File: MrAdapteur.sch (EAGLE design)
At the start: 12 parts, among them J1 PIN2F061.080, J2 PIN2F061.080, X1 1751248

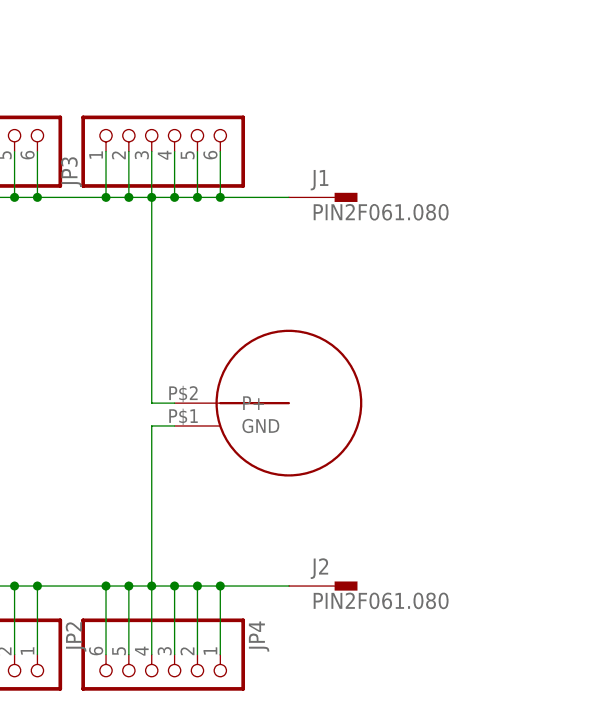
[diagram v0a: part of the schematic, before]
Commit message: Added standard DC jack, 4.75mm flat connector and wire loop for attaching alligator clips or scope probes
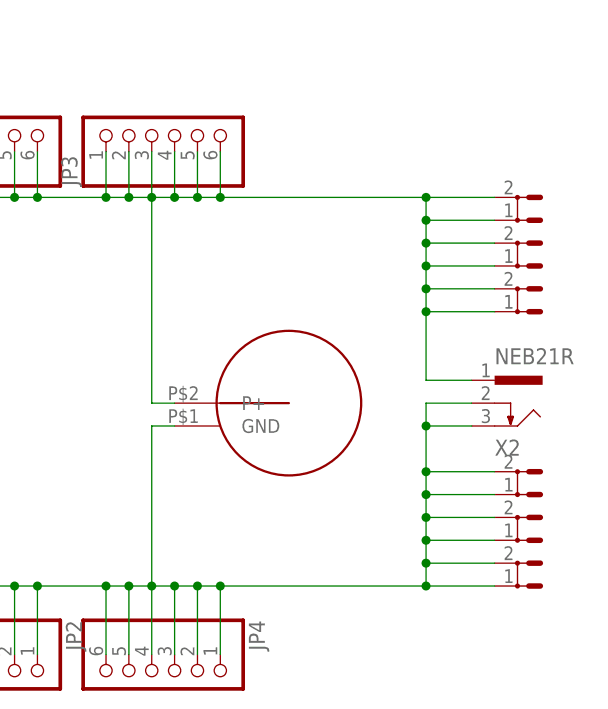
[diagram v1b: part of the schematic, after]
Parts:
- removed J1, J2: PIN2F061.080, con-faston:PIN2F061.080
- added X2: NEB21R, con-lumberg:NEB21R
- added X3, X4, X5, X6, X7, X8: (no value), con-rib:ST4,8
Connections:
- net N$1: now also X2.1, X3.1, X3.2, X5.1, X5.2, X7.1, X7.2; no longer J1.1
- net N$3: now also X2.2, X2.3, X4.1, X4.2, X6.1, X6.2, X8.1, X8.2; no longer J2.1
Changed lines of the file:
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@@
 <attribute name="OC_TME" value="ZL262-6SG"/>
 </part>
-<part name="J1" library="con-faston" deviceset="PIN2" device="F061.080">
-<attribute name="OC_TME" value="FS1536"/>
-</part>
-<part name="J2" library="con-faston" deviceset="PIN2" device="F061.080">
-<attribute name="OC_TME" value="FS1536"/>
-</part>
 <part name="X1" library="con-phoenix-350" deviceset="1751248" device=""/>
+<part name="X2" library="con-lumberg" deviceset="NEB21R" device=""/>
+<part name="X3" library="con-rib" deviceset="ST4,8" device=""/>
+<part name="X4" library="con-rib" deviceset="ST4,8" device=""/>
+<part name="X5" library="con-rib" deviceset="ST4,8" device=""/>
+<part name="X6" library="con-rib" deviceset="ST4,8" device=""/>
+<part name="X7" library="con-rib" deviceset="ST4,8" device=""/>
+<part name="X8" library="con-rib" deviceset="ST4,8" device=""/>
 </parts>
 <sheets>
@@
 <attribute name="OC_TME" x="116.84" y="30.48" size="1.778" layer="96" rot="R270" display="off"/>
 </instance>
-<instance part="J1" gate="-1" x="137.16" y="83.82">
-<attribute name="OC_TME" x="137.16" y="83.82" size="1.778" layer="96" display="off"/>
-</instance>
-<instance part="J2" gate="-1" x="137.16" y="40.64">
-<attribute name="OC_TME" x="137.16" y="40.64" size="1.778" layer="96" display="off"/>
-</instance>
 <instance part="X1" gate="-1" x="40.64" y="83.82" rot="R180"/>
 <instance part="X1" gate="-2" x="40.64" y="40.64" rot="R180"/>
+<instance part="X2" gate="G$1" x="157.48" y="60.96" rot="MR180"/>
+<instance part="X3" gate="-1" x="160.02" y="78.74" smashed="yes" rot="R180">
+<attribute name="VALUE" x="160.02" y="81.153" size="1.778" layer="96" rot="R180"/>
+</instance>
+<instance part="X4" gate="-1" x="160.02" y="48.26" smashed="yes" rot="R180">
+<attribute name="VALUE" x="160.02" y="50.673" size="1.778" layer="96" rot="R180"/>
+</instance>
+<instance part="X5" gate="-1" x="160.02" y="73.66" smashed="yes" rot="R180">
+<attribute name="VALUE" x="160.02" y="76.073" size="1.778" layer="96" rot="R180"/>
+</instance>
+<instance part="X6" gate="-1" x="160.02" y="53.34" smashed="yes" rot="R180">
+<attribute name="VALUE" x="160.02" y="55.753" size="1.778" layer="96" rot="R180"/>
+</instance>
+<instance part="X7" gate="-1" x="160.02" y="83.82" smashed="yes" rot="R180">
+<attribute name="VALUE" x="160.02" y="86.233" size="1.778" layer="96" rot="R180"/>
+</instance>
+<instance part="X8" gate="-1" x="160.02" y="43.18" smashed="yes" rot="R180">
+<attribute name="VALUE" x="160.02" y="45.593" size="1.778" layer="96" rot="R180"/>
+</instance>
 </instances>
 <busses>
@@
 <wire x1="114.3" y1="88.9" x2="114.3" y2="83.82" width="0.1524" layer="91"/>
 <junction x="114.3" y="83.82"/>
-<pinref part="J1" gate="-1" pin="1"/>
-<wire x1="124.46" y1="83.82" x2="132.08" y2="83.82" width="0.1524" layer="91"/>
+<wire x1="124.46" y1="83.82" x2="147.32" y2="83.82" width="0.1524" layer="91"/>
 <junction x="124.46" y="83.82"/>
 <pinref part="X1" gate="-1" pin="K"/>
 <junction x="43.18" y="83.82"/>
+<pinref part="X2" gate="G$1" pin="1"/>
+<wire x1="147.32" y1="83.82" x2="154.94" y2="83.82" width="0.1524" layer="91"/>
+<wire x1="152.4" y1="63.5" x2="147.32" y2="63.5" width="0.1524" layer="91"/>
+<wire x1="147.32" y1="63.5" x2="147.32" y2="71.12" width="0.1524" layer="91"/>
+<junction x="147.32" y="83.82"/>
+<pinref part="X3" gate="-1" pin="2"/>
+<wire x1="147.32" y1="71.12" x2="147.32" y2="73.66" width="0.1524" layer="91"/>
+<wire x1="147.32" y1="73.66" x2="147.32" y2="76.2" width="0.1524" layer="91"/>
+<wire x1="147.32" y1="76.2" x2="147.32" y2="78.74" width="0.1524" layer="91"/>
+<wire x1="147.32" y1="78.74" x2="147.32" y2="81.28" width="0.1524" layer="91"/>
+<wire x1="147.32" y1="81.28" x2="147.32" y2="83.82" width="0.1524" layer="91"/>
+<wire x1="154.94" y1="78.74" x2="147.32" y2="78.74" width="0.1524" layer="91"/>
+<junction x="147.32" y="78.74"/>
+<pinref part="X3" gate="-1" pin="1"/>
+<wire x1="154.94" y1="76.2" x2="147.32" y2="76.2" width="0.1524" layer="91"/>
+<junction x="147.32" y="76.2"/>
+<pinref part="X5" gate="-1" pin="2"/>
+<wire x1="154.94" y1="73.66" x2="147.32" y2="73.66" width="0.1524" layer="91"/>
+<junction x="147.32" y="73.66"/>
+<pinref part="X5" gate="-1" pin="1"/>
+<wire x1="154.94" y1="71.12" x2="147.32" y2="71.12" width="0.1524" layer="91"/>
+<junction x="147.32" y="71.12"/>
+<pinref part="X7" gate="-1" pin="2"/>
+<pinref part="X7" gate="-1" pin="1"/>
+<wire x1="154.94" y1="81.28" x2="147.32" y2="81.28" width="0.1524" layer="91"/>
+<junction x="147.32" y="81.28"/>
 </segment>
 </net>
@@
 <pinref part="JP4" gate="A" pin="1"/>
 <wire x1="124.46" y1="33.02" x2="124.46" y2="40.64" width="0.1524" layer="91"/>
-<pinref part="J2" gate="-1" pin="1"/>
-<wire x1="124.46" y1="40.64" x2="132.08" y2="40.64" width="0.1524" layer="91"/>
+<wire x1="124.46" y1="40.64" x2="147.32" y2="40.64" width="0.1524" layer="91"/>
 <junction x="124.46" y="40.64"/>
 <pinref part="X1" gate="-2" pin="K"/>
 <junction x="43.18" y="40.64"/>
+<pinref part="X2" gate="G$1" pin="2"/>
+<wire x1="147.32" y1="40.64" x2="154.94" y2="40.64" width="0.1524" layer="91"/>
+<wire x1="152.4" y1="60.96" x2="147.32" y2="60.96" width="0.1524" layer="91"/>
+<wire x1="147.32" y1="60.96" x2="147.32" y2="58.42" width="0.1524" layer="91"/>
+<junction x="147.32" y="40.64"/>
+<pinref part="X2" gate="G$1" pin="3"/>
+<wire x1="147.32" y1="58.42" x2="147.32" y2="53.34" width="0.1524" layer="91"/>
+<wire x1="147.32" y1="53.34" x2="147.32" y2="50.8" width="0.1524" layer="91"/>
+<wire x1="147.32" y1="50.8" x2="147.32" y2="48.26" width="0.1524" layer="91"/>
+<wire x1="147.32" y1="48.26" x2="147.32" y2="45.72" width="0.1524" layer="91"/>
+<wire x1="147.32" y1="45.72" x2="147.32" y2="43.18" width="0.1524" layer="91"/>
+<wire x1="147.32" y1="43.18" x2="147.32" y2="40.64" width="0.1524" layer="91"/>
+<wire x1="152.4" y1="58.42" x2="147.32" y2="58.42" width="0.1524" layer="91"/>
+<junction x="147.32" y="58.42"/>
+<pinref part="X4" gate="-1" pin="2"/>
+<wire x1="154.94" y1="48.26" x2="147.32" y2="48.26" width="0.1524" layer="91"/>
+<junction x="147.32" y="48.26"/>
+<pinref part="X4" gate="-1" pin="1"/>
+<wire x1="154.94" y1="45.72" x2="147.32" y2="45.72" width="0.1524" layer="91"/>
+<junction x="147.32" y="45.72"/>
+<pinref part="X6" gate="-1" pin="2"/>
+<wire x1="154.94" y1="53.34" x2="147.32" y2="53.34" width="0.1524" layer="91"/>
+<junction x="147.32" y="53.34"/>
+<pinref part="X6" gate="-1" pin="1"/>
+<wire x1="154.94" y1="50.8" x2="147.32" y2="50.8" width="0.1524" layer="91"/>
+<junction x="147.32" y="50.8"/>
+<pinref part="X8" gate="-1" pin="2"/>
+<wire x1="154.94" y1="43.18" x2="147.32" y2="43.18" width="0.1524" layer="91"/>
+<junction x="147.32" y="43.18"/>
+<pinref part="X8" gate="-1" pin="1"/>
 </segment>
 </net>

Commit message: Replaced DC connector with the adafruit one for bigger holes
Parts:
- removed X2: NEB21R, con-lumberg:NEB21R
- added U$6: 2.1MMJACKTHM, adafruit:2.1MMJACKTHM
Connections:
- net N$1: now also U$6.TIP; no longer X2.1
- net N$3: now also U$6.RING, U$6.RING_SW; no longer X2.2, X2.3
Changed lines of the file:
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@@
 <layer number="48" name="Document" color="7" fill="1" visible="no" active="no"/>
 <layer number="49" name="Reference" color="7" fill="1" visible="no" active="no"/>
+<layer number="50" name="dxf" color="7" fill="1" visible="no" active="no"/>
 <layer number="51" name="tDocu" color="7" fill="1" visible="no" active="no"/>
 <layer number="52" name="bDocu" color="7" fill="1" visible="no" active="no"/>
+<layer number="53" name="tGND_GNDA" color="7" fill="9" visible="no" active="no"/>
+<layer number="54" name="bGND_GNDA" color="1" fill="9" visible="no" active="no"/>
+<layer number="56" name="wert" color="7" fill="1" visible="no" active="no"/>
+<layer number="57" name="tCAD" color="7" fill="1" visible="no" active="no"/>
 <layer number="91" name="Nets" color="2" fill="1" visible="yes" active="yes"/>
 <layer number="92" name="Busses" color="1" fill="1" visible="yes" active="yes"/>
@@
 <layer number="97" name="Info" color="7" fill="1" visible="yes" active="yes"/>
 <layer number="98" name="Guide" color="6" fill="1" visible="yes" active="yes"/>
+<layer number="100" name="Muster" color="7" fill="1" visible="no" active="no"/>
+<layer number="101" name="Patch_Top" color="12" fill="4" visible="yes" active="yes"/>
+<layer number="102" name="Vscore" color="7" fill="1" visible="yes" active="yes"/>
+<layer number="103" name="fp3" color="7" fill="1" visible="no" active="yes"/>
+<layer number="104" name="Name" color="7" fill="1" visible="yes" active="yes"/>
+<layer number="105" name="Beschreib" color="9" fill="1" visible="yes" active="yes"/>
+<layer number="106" name="BGA-Top" color="4" fill="1" visible="yes" active="yes"/>
+<layer number="107" name="BD-Top" color="5" fill="1" visible="yes" active="yes"/>
+<layer number="108" name="fp8" color="7" fill="1" visible="no" active="yes"/>
+<layer number="109" name="fp9" color="7" fill="1" visible="no" active="yes"/>
+<layer number="110" name="fp0" color="7" fill="1" visible="no" active="yes"/>
+<layer number="111" name="LPC17xx" color="7" fill="1" visible="yes" active="yes"/>
+<layer number="112" name="tSilk" color="7" fill="1" visible="yes" active="yes"/>
+<layer number="116" name="Patch_BOT" color="9" fill="4" visible="yes" active="yes"/>
+<layer number="121" name="_tsilk" color="7" fill="1" visible="yes" active="yes"/>
+<layer number="122" name="_bsilk" color="7" fill="1" visible="yes" active="yes"/>
+<layer number="123" name="tTestmark" color="7" fill="1" visible="no" active="yes"/>
+<layer number="124" name="bTestmark" color="7" fill="1" visible="no" active="yes"/>
+<layer number="125" name="_tNames" color="7" fill="1" visible="yes" active="yes"/>
+<layer number="126" name="_bNames" color="7" fill="1" visible="yes" active="yes"/>
+<layer number="127" name="_tValues" color="7" fill="1" visible="yes" active="yes"/>
+<layer number="128" name="_bValues" color="7" fill="1" visible="yes" active="yes"/>
+<layer number="131" name="tAdjust" color="7" fill="1" visible="no" active="yes"/>
+<layer number="132" name="bAdjust" color="7" fill="1" visible="no" active="yes"/>
+<layer number="144" name="Drill_legend" color="7" fill="1" visible="yes" active="yes"/>
+<layer number="150" name="Notes" color="7" fill="1" visible="no" active="yes"/>
+<layer number="151" name="HeatSink" color="7" fill="1" visible="yes" active="yes"/>
+<layer number="152" name="_bDocu" color="7" fill="1" visible="yes" active="yes"/>
+<layer number="153" name="FabDoc1" color="6" fill="1" visible="no" active="no"/>
+<layer number="154" name="FabDoc2" color="2" fill="1" visible="no" active="no"/>
+<layer number="155" name="FabDoc3" color="7" fill="15" visible="no" active="no"/>
+<layer number="199" name="Contour" color="7" fill="1" visible="yes" active="yes"/>
+<layer number="200" name="200bmp" color="1" fill="10" visible="yes" active="yes"/>
+<layer number="201" name="201bmp" color="2" fill="1" visible="no" active="no"/>
+<layer number="202" name="202bmp" color="3" fill="1" visible="no" active="no"/>
+<layer number="203" name="203bmp" color="4" fill="10" visible="yes" active="yes"/>
+<layer number="204" name="204bmp" color="5" fill="10" visible="yes" active="yes"/>
+<layer number="205" name="205bmp" color="6" fill="10" visible="yes" active="yes"/>
+<layer number="206" name="206bmp" color="7" fill="10" visible="yes" active="yes"/>
+<layer number="207" name="207bmp" color="8" fill="10" visible="yes" active="yes"/>
+<layer number="208" name="208bmp" color="9" fill="10" visible="yes" active="yes"/>
+<layer number="209" name="209bmp" color="7" fill="1" visible="no" active="yes"/>
+<layer number="210" name="210bmp" color="7" fill="1" visible="no" active="yes"/>
+<layer number="211" name="211bmp" color="7" fill="1" visible="yes" active="yes"/>
+<layer number="212" name="212bmp" color="7" fill="1" visible="yes" active="yes"/>
+<layer number="213" name="213bmp" color="7" fill="1" visible="yes" active="yes"/>
+<layer number="214" name="214bmp" color="7" fill="1" visible="yes" active="yes"/>
+<layer number="215" name="215bmp" color="7" fill="1" visible="yes" active="yes"/>
+<layer number="216" name="216bmp" color="7" fill="1" visible="yes" active="yes"/>
+<layer number="217" name="217bmp" color="18" fill="1" visible="no" active="no"/>
+<layer number="218" name="218bmp" color="19" fill="1" visible="no" active="no"/>
+<layer number="219" name="219bmp" color="20" fill="1" visible="no" active="no"/>
+<layer number="220" name="220bmp" color="21" fill="1" visible="no" active="no"/>
+<layer number="221" name="221bmp" color="22" fill="1" visible="no" active="no"/>
+<layer number="222" name="222bmp" color="23" fill="1" visible="no" active="no"/>
+<layer number="223" name="223bmp" color="24" fill="1" visible="no" active="no"/>
+<layer number="224" name="224bmp" color="25" fill="1" visible="no" active="no"/>
+<layer number="248" name="Housing" color="7" fill="1" visible="yes" active="yes"/>
+<layer number="249" name="Edge" color="7" fill="1" visible="yes" active="yes"/>
+<layer number="250" name="Descript" color="7" fill="1" visible="no" active="no"/>
+<layer number="251" name="SMDround" color="7" fill="1" visible="no" active="no"/>
+<layer number="254" name="cooling" color="7" fill="1" visible="yes" active="yes"/>
 </layers>
 <schematic xreflabel="%F%N/%S.%C%R" xrefpart="/%S.%C%R">
@@
 </part>
 <part name="X1" library="con-phoenix-350" deviceset="1751248" device=""/>
-<part name="X2" library="con-lumberg" deviceset="NEB21R" device=""/>
 <part name="X3" library="con-rib" deviceset="ST4,8" device=""/>
 <part name="X4" library="con-rib" deviceset="ST4,8" device=""/>
@@
 <part name="X7" library="con-rib" deviceset="ST4,8" device=""/>
 <part name="X8" library="con-rib" deviceset="ST4,8" device=""/>
+<part name="U$6" library="adafruit" deviceset="2.1MMJACK" device="THM"/>
 </parts>
 <sheets>
@@
 <instance part="X1" gate="-1" x="40.64" y="83.82" rot="R180"/>
 <instance part="X1" gate="-2" x="40.64" y="40.64" rot="R180"/>
-<instance part="X2" gate="G$1" x="157.48" y="60.96" rot="MR180"/>
 <instance part="X3" gate="-1" x="160.02" y="78.74" smashed="yes" rot="R180">
 <attribute name="VALUE" x="160.02" y="81.153" size="1.778" layer="96" rot="R180"/>
@@
 <attribute name="VALUE" x="160.02" y="45.593" size="1.778" layer="96" rot="R180"/>
 </instance>
+<instance part="U$6" gate="G$1" x="157.48" y="60.96" rot="MR0"/>
 </instances>
 <busses>
@@
 <pinref part="X1" gate="-1" pin="K"/>
 <junction x="43.18" y="83.82"/>
-<pinref part="X2" gate="G$1" pin="1"/>
 <wire x1="147.32" y1="83.82" x2="154.94" y2="83.82" width="0.1524" layer="91"/>
 <wire x1="152.4" y1="63.5" x2="147.32" y2="63.5" width="0.1524" layer="91"/>
@@
 <wire x1="154.94" y1="81.28" x2="147.32" y2="81.28" width="0.1524" layer="91"/>
 <junction x="147.32" y="81.28"/>
+<pinref part="U$6" gate="G$1" pin="TIP"/>
 </segment>
 </net>
@@
 <pinref part="X1" gate="-2" pin="K"/>
 <junction x="43.18" y="40.64"/>
-<pinref part="X2" gate="G$1" pin="2"/>
 <wire x1="147.32" y1="40.64" x2="154.94" y2="40.64" width="0.1524" layer="91"/>
 <wire x1="152.4" y1="60.96" x2="147.32" y2="60.96" width="0.1524" layer="91"/>
 <wire x1="147.32" y1="60.96" x2="147.32" y2="58.42" width="0.1524" layer="91"/>
 <junction x="147.32" y="40.64"/>
-<pinref part="X2" gate="G$1" pin="3"/>
 <wire x1="147.32" y1="58.42" x2="147.32" y2="53.34" width="0.1524" layer="91"/>
 <wire x1="147.32" y1="53.34" x2="147.32" y2="50.8" width="0.1524" layer="91"/>
@@
 <junction x="147.32" y="43.18"/>
 <pinref part="X8" gate="-1" pin="1"/>
+<pinref part="U$6" gate="G$1" pin="RING"/>
+<pinref part="U$6" gate="G$1" pin="RING_SW"/>
 </segment>
 </net>

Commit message: Several minor fixes (sorry, can't remember them) ;)
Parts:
- removed X7, X8: (no value), con-rib:ST4,8
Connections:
- net N$1: no longer X7.1, X7.2
- net N$3: no longer X8.1, X8.2
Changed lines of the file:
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@@
 <part name="X5" library="con-rib" deviceset="ST4,8" device=""/>
 <part name="X6" library="con-rib" deviceset="ST4,8" device=""/>
-<part name="X7" library="con-rib" deviceset="ST4,8" device=""/>
-<part name="X8" library="con-rib" deviceset="ST4,8" device=""/>
 <part name="U$6" library="adafruit" deviceset="2.1MMJACK" device="THM"/>
 </parts>
@@
 <instance part="X6" gate="-1" x="160.02" y="53.34" smashed="yes" rot="R180">
 <attribute name="VALUE" x="160.02" y="55.753" size="1.778" layer="96" rot="R180"/>
-</instance>
-<instance part="X7" gate="-1" x="160.02" y="83.82" smashed="yes" rot="R180">
-<attribute name="VALUE" x="160.02" y="86.233" size="1.778" layer="96" rot="R180"/>
-</instance>
-<instance part="X8" gate="-1" x="160.02" y="43.18" smashed="yes" rot="R180">
-<attribute name="VALUE" x="160.02" y="45.593" size="1.778" layer="96" rot="R180"/>
 </instance>
 <instance part="U$6" gate="G$1" x="157.48" y="60.96" rot="MR0"/>
@@
 <wire x1="154.94" y1="71.12" x2="147.32" y2="71.12" width="0.1524" layer="91"/>
 <junction x="147.32" y="71.12"/>
-<pinref part="X7" gate="-1" pin="2"/>
-<pinref part="X7" gate="-1" pin="1"/>
 <wire x1="154.94" y1="81.28" x2="147.32" y2="81.28" width="0.1524" layer="91"/>
 <junction x="147.32" y="81.28"/>
@@
 <wire x1="154.94" y1="50.8" x2="147.32" y2="50.8" width="0.1524" layer="91"/>
 <junction x="147.32" y="50.8"/>
-<pinref part="X8" gate="-1" pin="2"/>
 <wire x1="154.94" y1="43.18" x2="147.32" y2="43.18" width="0.1524" layer="91"/>
 <junction x="147.32" y="43.18"/>
-<pinref part="X8" gate="-1" pin="1"/>
 <pinref part="U$6" gate="G$1" pin="RING"/>
 <pinref part="U$6" gate="G$1" pin="RING_SW"/>

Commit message: Replaced via with proper solder point
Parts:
- added U$10, U$11, U$8, U$9: SOLPAD07, 4mm:SOLPAD07
- JP1, JP2: PRICE_25 (none) -> 0.045
- JP3, JP4: PRICE_10 (none) -> 0.114
- U$1: PRICE_10 (none) -> 0.3
- U$2: OC_REICHELT BB 4 RE -> BB 4 RT; PRICE_10 (none) -> 0.3
- U$3, U$4: PRICE_10 (none) -> 0.32
- U$5: PRICE_10 (none) -> 0.573
- U$6: OC_TME (none) -> PC-GK2.1; PRICE_10 (none) -> 0.167
- X1: OC_TME (none) -> TB-3.5-P-2P/BL; PRICE_10 (none) -> 0.155
- X3, X4: OC_REICHELT (none) -> FS-P 4,75; PRICE_10 (none) -> 0.04
- X5, X6: OC_REICHELT (none) -> FS-P 6,35; PRICE_10 (none) -> 0.05
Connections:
- net N$1: now also U$10.P$1, U$8.P$1
- net N$3: now also U$11.P$1, U$9.P$1
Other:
- note removed: "Case: TME CP-Z-75/B"
